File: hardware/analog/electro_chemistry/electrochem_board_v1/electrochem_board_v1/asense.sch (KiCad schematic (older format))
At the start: 1 part

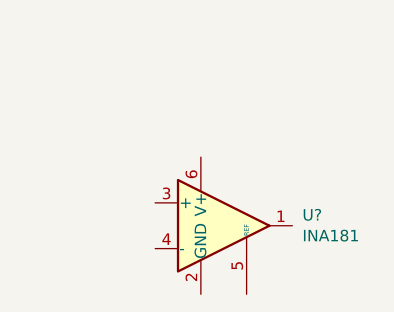
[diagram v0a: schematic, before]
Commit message: Electrochemistry board: thinking about current sense resistor
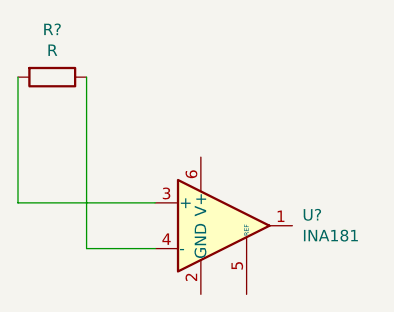
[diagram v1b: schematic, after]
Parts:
- added R?: R, symbol Device:R
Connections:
- net at U?.3 (+): now also R?.2
- net at U?.4 (-): now also R?.1
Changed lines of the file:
@@
 	1    0    0    -1
 $EndComp
+$Comp
+L Device:R R?
+U 1 1 609D8FAA
+P 4000 2700
+F 0 "R?" V 3793 2700 50  0000 C CNN
+F 1 "R" V 3884 2700 50  0000 C CNN
+F 2 "" V 3930 2700 50  0001 C CNN
+F 3 "~" H 4000 2700 50  0001 C CNN
+	1    4000 2700
+	0    1    1    0
+$EndComp
+Wire Wire Line
+	4150 2700 4150 3450
+Wire Wire Line
+	4150 3450 4450 3450
+Wire Wire Line
+	4450 3250 3850 3250
+Wire Wire Line
+	3850 3250 3850 2700
 $EndSCHEMATC

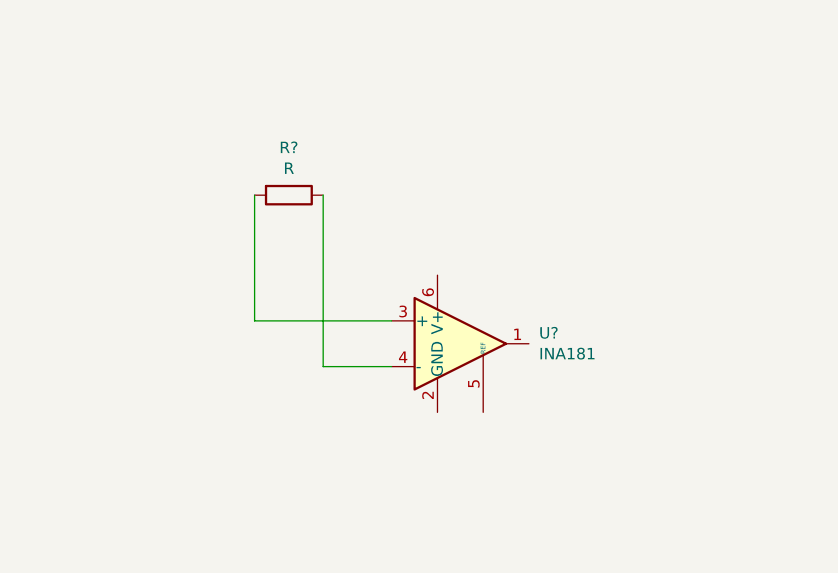
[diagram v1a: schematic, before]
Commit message: Electrochemistry board: preparing the layout
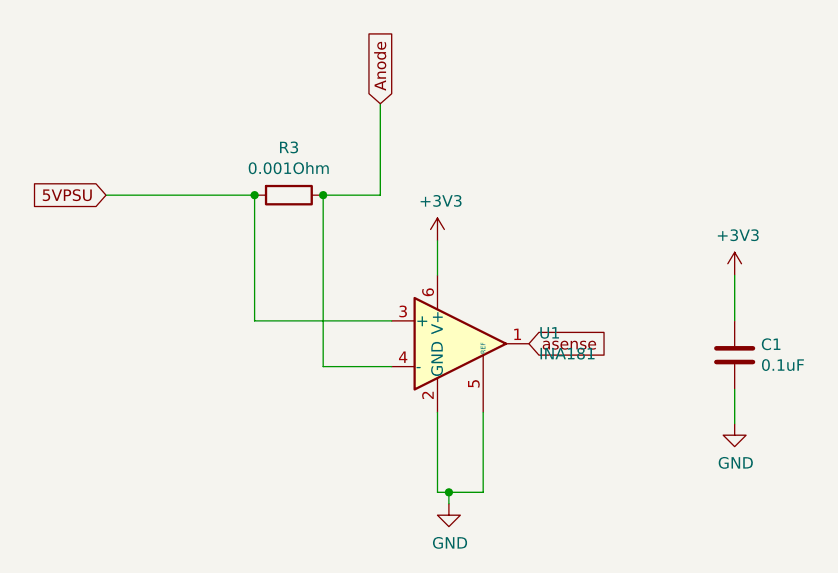
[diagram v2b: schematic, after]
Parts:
- added C1: 0.1uF, Capacitor_SMD:C_0402_1005Metric, symbol Device:C
- R3: renamed from R?; value R -> 0.001Ohm; footprint (none) -> Resistor_SMD:R_1206_3216Metric
- gave numbers to parts that had none: 1
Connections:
- net asense: now reaches U1.1
- net GND: now reaches U1.2 (GND)
- net GND: now also U1.5 (REF), C1.2
- net 5VPSU: now reaches R3.2, U1.3 (+)
- net Anode: now reaches R3.1, U1.4 (-)
- net +3V3: now reaches U1.6 (V+)
- net +3V3: now also C1.1
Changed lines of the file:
@@
 $EndDescr
 $Comp
-L Amplifier_Current:INA181 U?
+L Amplifier_Current:INA181 U1
 U 1 1 6096FFE7
 P 4750 3350
-F 0 "U?" H 5094 3396 50  0000 L CNN
+F 0 "U1" H 5094 3396 50  0000 L CNN
 F 1 "INA181" H 5094 3305 50  0000 L CNN
 F 2 "Package_TO_SOT_SMD:SOT-23-6" H 4800 3400 50  0001 C CNN
@@
 $EndComp
 $Comp
-L Device:R R?
+L Device:R R3
 U 1 1 609D8FAA
 P 4000 2700
-F 0 "R?" V 3793 2700 50  0000 C CNN
-F 1 "R" V 3884 2700 50  0000 C CNN
-F 2 "" V 3930 2700 50  0001 C CNN
+F 0 "R3" V 3793 2700 50  0000 C CNN
+F 1 "0.001Ohm" V 3884 2700 50  0000 C CNN
+F 2 "Resistor_SMD:R_1206_3216Metric" V 3930 2700 50  0001 C CNN
 F 3 "~" H 4000 2700 50  0001 C CNN
 	1    4000 2700
@@
 Wire Wire Line
 	3850 3250 3850 2700
+Text GLabel 5050 3350 2    50   Input ~ 0
+asense
+$Comp
+L power:GND #PWR07
+U 1 1 60A075D5
+P 4700 4050
+F 0 "#PWR07" H 4700 3800 50  0001 C CNN
+F 1 "GND" H 4705 3877 50  0000 C CNN
+F 2 "" H 4700 4050 50  0001 C CNN
+F 3 "" H 4700 4050 50  0001 C CNN
+	1    4700 4050
+	1    0    0    -1
+$EndComp
+Wire Wire Line
+	4650 3650 4650 4000
+Wire Wire Line
+	4650 4000 4700 4000
+Wire Wire Line
+	4700 4000 4700 4050
+Wire Wire Line
+	4850 3650 4850 4000
+Wire Wire Line
+	4850 4000 4700 4000
+Connection ~ 4700 4000
+$Comp
+L power:+3V3 #PWR06
+U 1 1 60A07A39
+P 4650 2900
+F 0 "#PWR06" H 4650 2750 50  0001 C CNN
+F 1 "+3V3" H 4665 3073 50  0000 C CNN
+F 2 "" H 4650 2900 50  0001 C CNN
+F 3 "" H 4650 2900 50  0001 C CNN
+	1    4650 2900
+	1    0    0    -1
+$EndComp
+Wire Wire Line
+	4650 2900 4650 3050
+$Comp
+L Device:C C1
+U 1 1 60A081FF
+P 5950 3400
+F 0 "C1" H 6065 3446 50  0000 L CNN
+F 1 "0.1uF" H 6065 3355 50  0000 L CNN
+F 2 "Capacitor_SMD:C_0402_1005Metric" H 5988 3250 50  0001 C CNN
+F 3 "~" H 5950 3400 50  0001 C CNN
+	1    5950 3400
+	1    0    0    -1
+$EndComp
+$Comp
+L power:GND #PWR09
+U 1 1 60A089EA
+P 5950 3700
+F 0 "#PWR09" H 5950 3450 50  0001 C CNN
+F 1 "GND" H 5955 3527 50  0000 C CNN
+F 2 "" H 5950 3700 50  0001 C CNN
+F 3 "" H 5950 3700 50  0001 C CNN
+	1    5950 3700
+	1    0    0    -1
+$EndComp
+$Comp
+L power:+3V3 #PWR08
+U 1 1 60A09244
+P 5950 3050
+F 0 "#PWR08" H 5950 2900 50  0001 C CNN
+F 1 "+3V3" H 5965 3223 50  0000 C CNN
+F 2 "" H 5950 3050 50  0001 C CNN
+F 3 "" H 5950 3050 50  0001 C CNN
+	1    5950 3050
+	1    0    0    -1
+$EndComp
+Wire Wire Line
+	5950 3050 5950 3250
+Wire Wire Line
+	5950 3550 5950 3700
+Text GLabel 3200 2700 0    50   Input ~ 0
+5VPSU
+Wire Wire Line
+	3200 2700 3850 2700
+Connection ~ 3850 2700
+Text GLabel 4400 2300 1    50   Input ~ 0
+Anode
+Wire Wire Line
+	4150 2700 4400 2700
+Wire Wire Line
+	4400 2700 4400 2300
+Connection ~ 4150 2700
 $EndSCHEMATC
